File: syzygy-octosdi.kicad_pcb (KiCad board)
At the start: 2 copper layers, 50 x 100 mm, 177 parts, among them CN1 QTH-020-01-F-D-DP-A, J1 Conn_02x03_Odd_Even, U1 LMH0344SQE_NOPB, U10 LMH0344SQE_NOPB, U11 STM32G031G8Ux, U2 LMH0344SQE_NOPB, U3 GS2988-INE3, U4 GS2988-INE3, U5 PCAL6416AHF, U6 PCAL6416AHF, U7 GS2988-INE3, U8 GS2988-INE3, U9 LMH0344SQE_NOPB, X1 SX7DF148_500B20F30DNN

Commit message: implement schematic review feedback
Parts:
- U3, U4, U7, U8: value GS2988-INE3 -> ~
- X1: value SX7DF148_500B20F30DNN -> ~

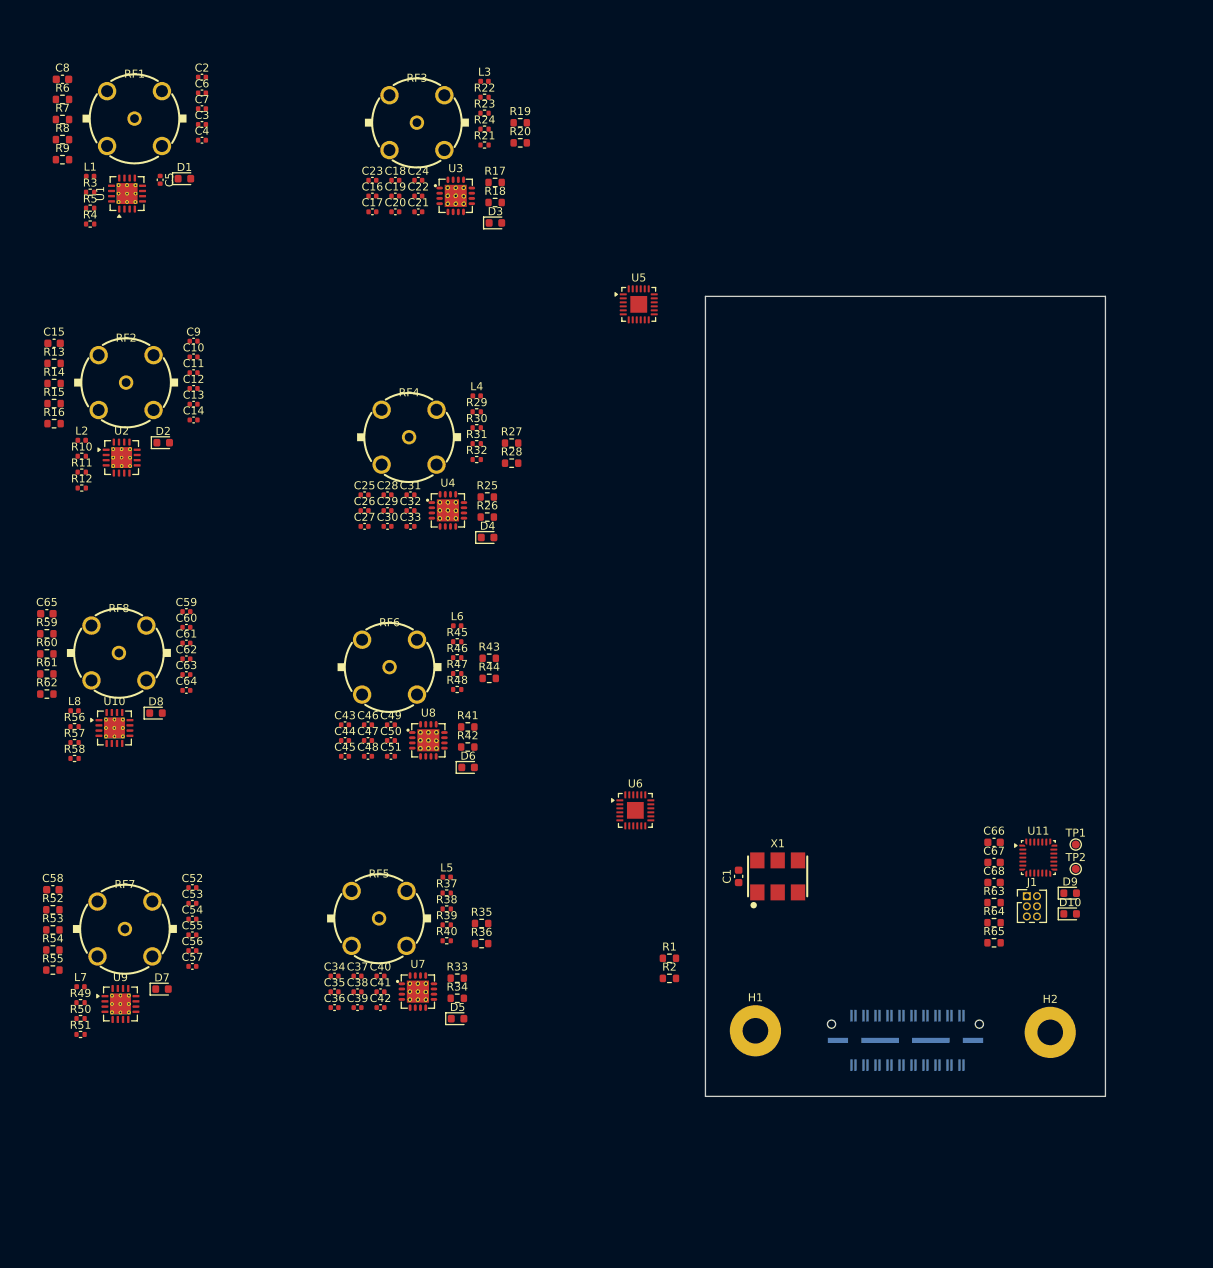
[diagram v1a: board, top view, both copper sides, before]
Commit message: substitute bnc connector for better max freq
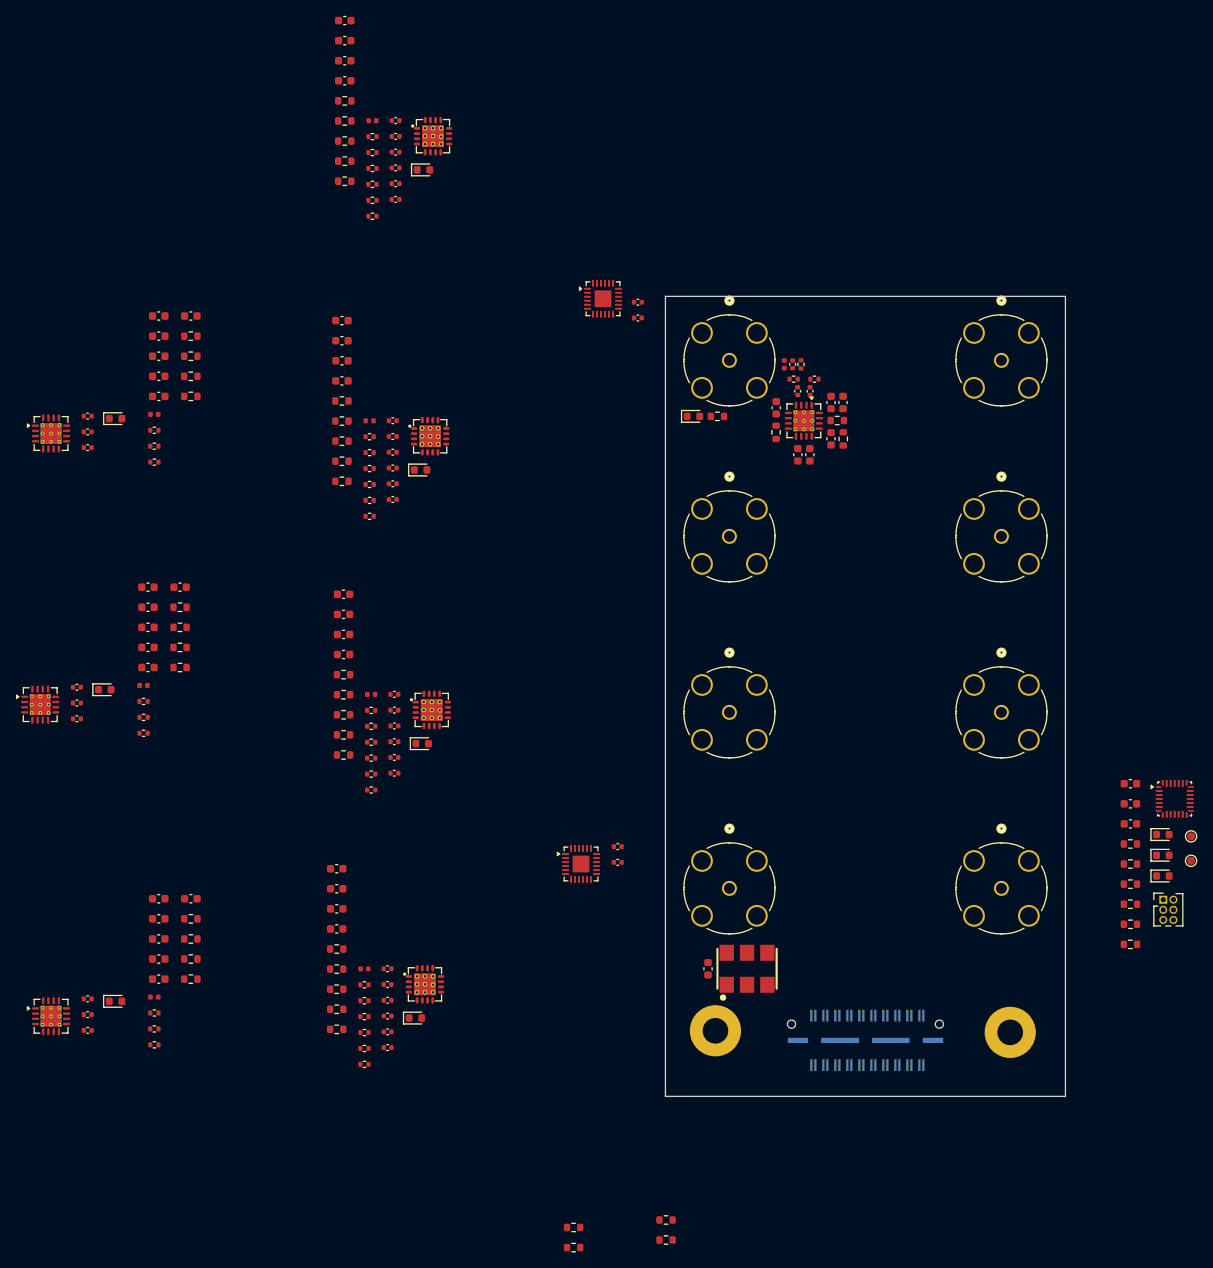
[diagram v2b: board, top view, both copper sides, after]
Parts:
- removed RF1, RF2, RF3, RF4, RF5, RF6, RF7, RF8: DOSIN-801-0057, JLCImport:DOSIN-801-0057
- added C10: 100n, Capacitor_SMD:C_0603_1608Metric, F.Cu at (120.7, 67.8)
- added C18: 100n, Capacitor_SMD:C_0603_1608Metric, F.Cu at (36.7, 62.5)
- added C19: 100n, Capacitor_SMD:C_0603_1608Metric, F.Cu at (40.7, 52.5)
- added C24: 100n, Capacitor_SMD:C_0402_1005Metric, F.Cu at (66.3, 37.9)
- added C34: 100n, Capacitor_SMD:C_0402_1005Metric, F.Cu at (65.9, 75.4)
- added C40: 100n, Capacitor_SMD:C_0402_1005Metric, F.Cu at (96.6, 50.7)
- added C41: 100n, Capacitor_SMD:C_0402_1005Metric, F.Cu at (96.6, 52.7)
- added C42: 100n, Capacitor_SMD:C_0402_1005Metric, F.Cu at (94.0, 118.8)
- added C43: 100n, Capacitor_SMD:C_0402_1005Metric, F.Cu at (94.0, 120.8)
- added C48: 100n, Capacitor_SMD:C_0402_1005Metric, F.Cu at (65.3, 143.9)
- added C58: 100n, Capacitor_SMD:C_0402_1005Metric, F.Cu at (66.1, 109.6)
- added C71: 100n, Capacitor_SMD:C_0603_1608Metric, F.Cu at (36.7, 135.3)
- added C72: 100n, Capacitor_SMD:C_0603_1608Metric, F.Cu at (40.7, 125.3)
- added C80: 100n, Capacitor_SMD:C_0603_1608Metric, F.Cu at (35.3, 96.4)
- added C81: 100n, Capacitor_SMD:C_0603_1608Metric, F.Cu at (39.3, 86.3)
- added C9: 100n, Capacitor_SMD:C_0603_1608Metric, F.Cu at (120.7, 63.3)
- added D11: LED, LED_SMD:LED_0603_1608Metric, F.Cu at (162.2, 122.5)
- added J1: Conn_Coaxial, JLCImport:CONN_73171-1900_MOL, F.Cu at (108.0, 58.0)
- added J10: Conn_Coaxial, JLCImport:CONN_73171-1900_MOL, F.Cu at (142.0, 124.0)
- added J2: Conn_Coaxial, JLCImport:CONN_73171-1900_MOL, F.Cu at (142.0, 58.0)
- added J3: Conn_Coaxial, JLCImport:CONN_73171-1900_MOL, F.Cu at (108.0, 80.0)
- added J5: Conn_Coaxial, JLCImport:CONN_73171-1900_MOL, F.Cu at (142.0, 80.0)
- added J6: Conn_Coaxial, JLCImport:CONN_73171-1900_MOL, F.Cu at (108.0, 102.0)
- added J7: Conn_Coaxial, JLCImport:CONN_73171-1900_MOL, F.Cu at (142.0, 102.0)
- added J8: Conn_Coaxial, JLCImport:CONN_73171-1900_MOL, F.Cu at (108.0, 124.0)
- added R19: 49.9, Resistor_SMD:R_0402_1005Metric, F.Cu at (63.4, 38.0)
- added R2: 10k, Resistor_SMD:R_0603_1608Metric, F.Cu at (88.5, 168.9)
- added R20: 49.9, Resistor_SMD:R_0402_1005Metric, F.Cu at (63.4, 40.0)
- added R27: 10k, Resistor_SMD:R_0603_1608Metric, F.Cu at (59.9, 35.6)
- added R30: 49.9, Resistor_SMD:R_0402_1005Metric, F.Cu at (63.0, 75.5)
- added R31: 49.9, Resistor_SMD:R_0402_1005Metric, F.Cu at (63.0, 77.5)
- added R38: 10k, Resistor_SMD:R_0603_1608Metric, F.Cu at (59.6, 73.1)
- added R4: 10k, Resistor_SMD:R_0603_1608Metric, F.Cu at (88.5, 166.4)
- added R41: 49.9, Resistor_SMD:R_0402_1005Metric, F.Cu at (62.4, 144.0)
- added R42: 49.9, Resistor_SMD:R_0402_1005Metric, F.Cu at (62.4, 146.0)
- added R49: 10k, Resistor_SMD:R_0603_1608Metric, F.Cu at (58.9, 141.6)
- added R52: 49.9, Resistor_SMD:R_0402_1005Metric, F.Cu at (63.2, 109.7)
- added R53: 49.9, Resistor_SMD:R_0402_1005Metric, F.Cu at (63.2, 111.7)
- added R60: 10k, Resistor_SMD:R_0603_1608Metric, F.Cu at (59.8, 107.3)
- added R80: 10k, Resistor_SMD:R_0603_1608Metric, F.Cu at (158.1, 128.5)
- added R81: 10k, Resistor_SMD:R_0603_1608Metric, F.Cu at (158.1, 126.0)
- added R82: 4k7, Resistor_SMD:R_0603_1608Metric, F.Cu at (158.1, 131.0)
- C1: value 10n -> 100n
- C14: renamed from C12; value 100n -> 1u; footprint Capacitor_SMD:C_0402_1005Metric -> Capacitor_SMD:C_0603_1608Metric
- C15: renamed from C13; footprint Capacitor_SMD:C_0402_1005Metric -> Capacitor_SMD:C_0603_1608Metric
- C16: renamed from C14; footprint Capacitor_SMD:C_0402_1005Metric -> Capacitor_SMD:C_0603_1608Metric
- C22: renamed from C18; footprint Capacitor_SMD:C_0402_1005Metric -> Capacitor_SMD:C_0603_1608Metric
- C23: renamed from C19; footprint Capacitor_SMD:C_0402_1005Metric -> Capacitor_SMD:C_0603_1608Metric
- C25: renamed from C20; footprint Capacitor_SMD:C_0402_1005Metric -> Capacitor_SMD:C_0603_1608Metric
- C29: renamed from C24; footprint Capacitor_SMD:C_0402_1005Metric -> Capacitor_SMD:C_0603_1608Metric
- C32: renamed from C27; footprint Capacitor_SMD:C_0402_1005Metric -> Capacitor_SMD:C_0603_1608Metric
- C33: renamed from C28; footprint Capacitor_SMD:C_0402_1005Metric -> Capacitor_SMD:C_0603_1608Metric
- C35: renamed from C29; footprint Capacitor_SMD:C_0402_1005Metric -> Capacitor_SMD:C_0603_1608Metric
- C39: renamed from C33; footprint Capacitor_SMD:C_0402_1005Metric -> Capacitor_SMD:C_0603_1608Metric
- C46: renamed from C36; footprint Capacitor_SMD:C_0402_1005Metric -> Capacitor_SMD:C_0603_1608Metric
- C47: renamed from C37; footprint Capacitor_SMD:C_0402_1005Metric -> Capacitor_SMD:C_0603_1608Metric
- C49: renamed from C38; footprint Capacitor_SMD:C_0402_1005Metric -> Capacitor_SMD:C_0603_1608Metric
- C5: value 100n -> 1u; footprint Capacitor_SMD:C_0402_1005Metric -> Capacitor_SMD:C_0603_1608Metric
- C53: renamed from C42; footprint Capacitor_SMD:C_0402_1005Metric -> Capacitor_SMD:C_0603_1608Metric
- C56: renamed from C45; footprint Capacitor_SMD:C_0402_1005Metric -> Capacitor_SMD:C_0603_1608Metric
- C57: renamed from C46; footprint Capacitor_SMD:C_0402_1005Metric -> Capacitor_SMD:C_0603_1608Metric
- C59: renamed from C47; footprint Capacitor_SMD:C_0402_1005Metric -> Capacitor_SMD:C_0603_1608Metric
- C6, C7: footprint Capacitor_SMD:C_0402_1005Metric -> Capacitor_SMD:C_0603_1608Metric
- C63: renamed from C51; footprint Capacitor_SMD:C_0402_1005Metric -> Capacitor_SMD:C_0603_1608Metric
- C67: renamed from C55; value 100n -> 1u; footprint Capacitor_SMD:C_0402_1005Metric -> Capacitor_SMD:C_0603_1608Metric
- C68: renamed from C56; footprint Capacitor_SMD:C_0402_1005Metric -> Capacitor_SMD:C_0603_1608Metric
- C69: renamed from C57; footprint Capacitor_SMD:C_0402_1005Metric -> Capacitor_SMD:C_0603_1608Metric
- C76: renamed from C62; value 100n -> 1u; footprint Capacitor_SMD:C_0402_1005Metric -> Capacitor_SMD:C_0603_1608Metric
- C77: renamed from C63; footprint Capacitor_SMD:C_0402_1005Metric -> Capacitor_SMD:C_0603_1608Metric
- C78: renamed from C64; footprint Capacitor_SMD:C_0402_1005Metric -> Capacitor_SMD:C_0603_1608Metric
- U3, U4, U7, U8: value ~ -> GS2988-INE3
- X1: value ~ -> SX7DF148_500B20F30DNN
- moved C8 105.6 mm to (122.2, 63.3), turned to 90 degrees
- moved R10 104.5 mm to (122.2, 67.8), turned to -90 degrees
- moved R11 102.2 mm to (121.5, 65.5)
- moved R9 97.4 mm to (113.8, 67.0), turned to -90 degrees
- moved R6 92.6 mm to (118.6, 60.4)
- moved R5 91.4 mm to (117.0, 58.5), turned to -90 degrees
- moved R8 91.0 mm to (106.5, 65.0), turned to 180 degrees
- moved R7 90.5 mm to (116.0, 60.4)
- moved L1 89.9 mm to (114.8, 58.5), turned to -90 degrees
- moved U1 89.2 mm to (117.3, 65.5), turned to -90 degrees
- moved C6 88.4 mm to (118.0, 69.8), turned to -90 degrees
- moved C7 86.1 mm to (116.5, 69.8), turned to -90 degrees
- moved C3 83.0 mm to (118.1, 61.9), turned to -90 degrees
- moved C5 82.1 mm to (113.8, 63.9)
- moved C2 82.1 mm to (115.9, 58.5), turned to -90 degrees
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- renumbered C9 to C11, C10 to C12, C11 to C13, C15 to C17, C16 to C20, C17 to C21, C21 to C26, C22 to C27, C23 to C28, C25 to C30, C26 to C31, C30 to C36, C31 to C37, C32 to C38, C34 to C44, C35 to C45, C39 to C50, C40 to C51, C41 to C52, C43 to C54, C44 to C55, C48 to C60, C49 to C61, C50 to C62, C52 to C64, C53 to C65, C54 to C66, C58 to C70, C59 to C73, C60 to C74, C61 to C75, C65 to C79, C66 to C82, C67 to C83, C68 to C84, J1 to J9, R8 to R10, R9 to R11, R10 to R12, R11 to R13, R12 to R14, R13 to R15, R14 to R16, R15 to R17, R16 to R18, R18 to R21, R17 to R22, R19 to R23, R20 to R24, R21 to R25, R22 to R26, R23 to R28, R24 to R29, R2 to R3, R26 to R32, R25 to R33, R27 to R34, R28 to R35, R29 to R36, R30 to R37, R31 to R39, R32 to R40, R34 to R43, R33 to R44, R35 to R45, R36 to R46, R37 to R47, R38 to R48, R3 to R5, R39 to R50, R40 to R51, R42 to R54, R41 to R55, R43 to R56, R44 to R57, R45 to R58, R46 to R59, R4 to R6, R47 to R61, R48 to R62, R49 to R63, R50 to R64, R51 to R65, R52 to R66, R53 to R67, R54 to R68, R55 to R69, R5 to R7, R56 to R70, R57 to R71, R58 to R72, R59 to R73, R60 to R74, R61 to R75, R62 to R76, R63 to R77, R64 to R78, R65 to R79, R6 to R8, R7 to R9
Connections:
- R10 pad 2: GND -> /~{VIO_GOOD}
- R17 pad 2: GND -> /~{VIO_GOOD}
- R68 pad 2: GND -> /~{VIO_GOOD}
- R75 pad 2: GND -> /~{VIO_GOOD}
- U11 pad 7: unconnected-(U11-PA1-Pad7) -> /VIO
- U11 pad 8: unconnected-(U11-PA2-Pad8) -> /VIO_GOOD
- U11 pad 9: unconnected-(U11-PA3-Pad9) -> /~{VIO_GOOD}
- U6 pad 18: /VIO -> +3V3
- X1 pad 1: unconnected-(X1-tri-state-Pad1) -> /VIO_GOOD

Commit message: split gpio expanders by inputs/outputs instead of quads
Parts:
- removed the C38 at (65.9, 73.4)
- removed the C39 at (59.6, 60.6)
- removed the C42 at (94.0, 118.8)
- removed the C43 at (94.0, 120.8)
- removed J10: Conn_Coaxial, JLCImport:CONN_73171-1900_MOL
- removed the R33 at (59.6, 63.1)
- removed the R34 at (59.6, 68.1)
- removed the R35 at (59.6, 70.6)
- removed the R36 at (63.0, 67.5)
- removed the R37 at (63.0, 69.5)
- removed the R38 at (59.6, 73.1)
- removed the R39 at (63.0, 71.5)
- removed the R40 at (63.0, 73.5)
- added C40: 100n, Capacitor_SMD:C_0402_1005Metric, F.Cu at (94.2, 102.9)
- added C41: 100n, Capacitor_SMD:C_0402_1005Metric, F.Cu at (94.2, 104.9)
- added C52: 10n, Capacitor_SMD:C_0402_1005Metric, F.Cu at (200.9, 78.9)
- added C53: 10n, Capacitor_SMD:C_0402_1005Metric, F.Cu at (200.9, 80.9)
- added J4: Conn_Coaxial, JLCImport:CONN_73171-1900_MOL, F.Cu at (243.1, 42.8)
- added R44: 49.9, Resistor_SMD:R_0402_1005Metric, F.Cu at (198.0, 80.9)
- added R45: 49.9, Resistor_SMD:R_0402_1005Metric, F.Cu at (198.0, 82.9)
- added R46: 1k, Resistor_SMD:R_0603_1608Metric, F.Cu at (194.5, 76.5)
- added R47: 750, Resistor_SMD:R_0603_1608Metric, F.Cu at (194.5, 79.0)
- added R48: 10k, Resistor_SMD:R_0603_1608Metric, F.Cu at (194.5, 81.5)
- added R49: 10k, Resistor_SMD:R_0603_1608Metric, F.Cu at (194.5, 84.0)
- added R50: 75, Resistor_SMD:R_0402_1005Metric, F.Cu at (198.0, 84.9)
- added R51: 75, Resistor_SMD:R_0402_1005Metric, F.Cu at (198.0, 86.9)
- C20, C60: value 10n -> C
- C21, C30, C31: value 10n -> 1u
- C22: value 4u7 -> 1u; footprint Capacitor_SMD:C_0603_1608Metric -> Capacitor_SMD:C_0402_1005Metric
- C23, C32, C35: value 4u7 -> 1u
- C24, C34: value 100n -> 4u7; footprint Capacitor_SMD:C_0402_1005Metric -> Capacitor_SMD:C_0603_1608Metric
- C26: value 10n -> 1u; footprint Capacitor_SMD:C_0402_1005Metric -> Capacitor_SMD:C_0603_1608Metric
- C27, C36, C37: value 10n -> 100n; footprint Capacitor_SMD:C_0402_1005Metric -> Capacitor_SMD:C_0603_1608Metric
- C28: value C -> 100n; footprint Capacitor_SMD:C_0402_1005Metric -> Capacitor_SMD:C_0603_1608Metric
- C29: value 4u7 -> C; footprint Capacitor_SMD:C_0603_1608Metric -> Capacitor_SMD:C_0402_1005Metric
- C54, C55, C61: value 10n -> 4u7; footprint Capacitor_SMD:C_0402_1005Metric -> Capacitor_SMD:C_0603_1608Metric
- C56: value 4u7 -> 100n; footprint Capacitor_SMD:C_0603_1608Metric -> Capacitor_SMD:C_0402_1005Metric
- C58: value 100n -> 10n
- C59, C63, C68, C69, C78: value 4u7 -> 10n; footprint Capacitor_SMD:C_0603_1608Metric -> Capacitor_SMD:C_0402_1005Metric
- C62, C73: value C -> 10n
- C64: value C -> 4u7; footprint Capacitor_SMD:C_0402_1005Metric -> Capacitor_SMD:C_0603_1608Metric
- C65, C74, C75: value 1u -> 4u7; footprint Capacitor_SMD:C_0402_1005Metric -> Capacitor_SMD:C_0603_1608Metric
- C66: value 1u -> 100n
- C67: value 1u -> 4u7
- C70: value 1u -> C; footprint Capacitor_SMD:C_0603_1608Metric -> Capacitor_SMD:C_0402_1005Metric
- C71, C81: value 100n -> 4u7
- C72: value 100n -> 10n; footprint Capacitor_SMD:C_0603_1608Metric -> Capacitor_SMD:C_0402_1005Metric
- C76: value 1u -> 100n; footprint Capacitor_SMD:C_0603_1608Metric -> Capacitor_SMD:C_0402_1005Metric
- C79: value 1u -> 10n; footprint Capacitor_SMD:C_0603_1608Metric -> Capacitor_SMD:C_0402_1005Metric
- C80: value 100n -> C; footprint Capacitor_SMD:C_0603_1608Metric -> Capacitor_SMD:C_0402_1005Metric
- L3, L4: value 5n6 -> 3n9
- L7, L8: value 3n9 -> 5n6
- R19, R20, R53: value 49.9 -> 75
- R21: value 1k -> 37.4; footprint Resistor_SMD:R_0603_1608Metric -> Resistor_SMD:R_0402_1005Metric
- R22: value 750 -> 1k
- R25: value 75 -> 0; footprint Resistor_SMD:R_0402_1005Metric -> Resistor_SMD:R_0603_1608Metric
- R27, R75: value 10k -> 75; footprint Resistor_SMD:R_0603_1608Metric -> Resistor_SMD:R_0402_1005Metric
- R28: value 75 -> 37.4
- R29: value 75 -> 1k; footprint Resistor_SMD:R_0402_1005Metric -> Resistor_SMD:R_0603_1608Metric
- R30, R31, R52: value 49.9 -> 10k; footprint Resistor_SMD:R_0402_1005Metric -> Resistor_SMD:R_0603_1608Metric
- R32: value 1k -> 0
- R54, R73: value 1k -> 75; footprint Resistor_SMD:R_0603_1608Metric -> Resistor_SMD:R_0402_1005Metric
- R55: value 750 -> 49.9; footprint Resistor_SMD:R_0603_1608Metric -> Resistor_SMD:R_0402_1005Metric
- R56, R67: value 10k -> 49.9; footprint Resistor_SMD:R_0603_1608Metric -> Resistor_SMD:R_0402_1005Metric
- R57, R68: value 10k -> 1k
- R58: value 75 -> 750; footprint Resistor_SMD:R_0402_1005Metric -> Resistor_SMD:R_0603_1608Metric
- R59, R63, R70, R71: value 75 -> 10k; footprint Resistor_SMD:R_0402_1005Metric -> Resistor_SMD:R_0603_1608Metric
- R65, R72: value 37.4 -> 75
- R66: value 1k -> 49.9; footprint Resistor_SMD:R_0603_1608Metric -> Resistor_SMD:R_0402_1005Metric
- R69: value 0 -> 750
- R76: value 0 -> 75; footprint Resistor_SMD:R_0603_1608Metric -> Resistor_SMD:R_0402_1005Metric
- U10, U9: value LMH0344SQE_NOPB -> GS2988-INE3; footprint Package_DFN_QFN:Texas_RUM0016A_WQFN-16-1EP_4x4mm_P0.65mm_EP2.6x2.6mm_ThermalVias -> JLCImport:GS2988-INE3
- U3, U4: value GS2988-INE3 -> LMH0344SQE_NOPB; footprint JLCImport:GS2988-INE3 -> Package_DFN_QFN:Texas_RUM0016A_WQFN-16-1EP_4x4mm_P0.65mm_EP2.6x2.6mm_ThermalVias
- moved U9 221.5 mm to (226.5, 52.2)
- moved C11 219.3 mm to (246.6, 78.9)
- moved C12 219.3 mm to (246.6, 80.9)
- moved C13 219.3 mm to (246.6, 82.9)
- moved C14 219.3 mm to (255.5, 66.4)
- moved C15 219.3 mm to (255.5, 68.9)
- moved C16 219.3 mm to (255.5, 71.4)
- moved C17 219.3 mm to (255.5, 73.9)
- moved C18 219.3 mm to (255.5, 76.5)
- moved L2 219.3 mm to (255.0, 78.7)
- moved R12 219.3 mm to (255.0, 80.7)
- moved R13 219.3 mm to (255.0, 82.7)
- moved R14 219.3 mm to (255.0, 84.7)
- moved U2 219.3 mm to (242.0, 81.1)
- moved C19 219.3 mm to (259.5, 66.4)
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- renumbered C40 to C38, C41 to C39, C44 to C42, C45 to C43, C46 to C44, C47 to C45, C48 to C46, C49 to C47, C50 to C48, C51 to C49, C52 to C50, C53 to C51, R41 to R33, R42 to R34, R43 to R35, R44 to R36, R45 to R37, R46 to R38, R47 to R39, R48 to R40, R49 to R41, R50 to R42, R51 to R43
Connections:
- net /Quad/SDI In 1/BYPASS renamed /Inputs/SDI In 1/BYPASS
- net /Quad/SDI In 1/MUTE renamed /Inputs/SDI In 1/MUTE
- net /Quad/SDI In 1/~{CD} renamed /Inputs/SDI In 1/~{CD}
- C20 pad 1: +3V3 -> Net-(J3-In)
- C20 pad 2: GND -> Net-(C20-Pad2)
- C21 pad 1: +3V3 -> Net-(C20-Pad2)
- C21 pad 2: GND -> Net-(U3-SDI)
- C22 pad 1: /TX0.P -> Net-(C22-Pad1)
- C22 pad 2: Net-(U3-DDI) -> Net-(U3-SDI#)
- C23 pad 1: /TX0.N -> Net-(U3-AEC+)
- C23 pad 2: Net-(U3-~{DDI}) -> Net-(U3-AEC-)
- C24 pad 1: Net-(C24-Pad1) -> Net-(U3-SDO)
- C24 pad 2: GND -> /RX2.P
- C25 pad 1: Net-(U3-~{SDO}) -> Net-(U3-SDO#)
- C25 pad 2: Net-(C25-Pad2) -> /RX2.N
- C28 pad 1: Net-(U3-SDO) -> +3V3
- C28 pad 2: Net-(C28-Pad2) -> GND
- C29 pad 1: Net-(C28-Pad2) -> Net-(J4-In)
- C29 pad 2: Net-(J3-In) -> Net-(C29-Pad2)
- C30 pad 1: +3V3 -> Net-(C29-Pad2)
- C30 pad 2: GND -> Net-(U4-SDI)
- C31 pad 1: +3V3 -> Net-(C31-Pad1)
- C31 pad 2: GND -> Net-(U4-SDI#)
- C32 pad 1: /TX1.P -> Net-(U4-AEC+)
- C32 pad 2: Net-(U4-DDI) -> Net-(U4-AEC-)
- C33 pad 1: /TX1.N -> Net-(U4-SDO)
- C33 pad 2: Net-(U4-~{DDI}) -> /RX3.P
- C34 pad 1: Net-(C34-Pad1) -> Net-(U4-SDO#)
- C34 pad 2: GND -> /RX3.N
- C35 pad 1: Net-(U4-~{SDO}) -> +3V3
- C35 pad 2: Net-(C35-Pad2) -> GND
- C44 pad 1: /TX3.P -> /TX0.P
- C45 pad 1: /TX3.N -> /TX0.N
- C54 pad 1: +3V3 -> /TX1.P
- C54 pad 2: GND -> Net-(U8-DDI)
- C55 pad 1: +3V3 -> /TX1.N
- C55 pad 2: GND -> Net-(U8-~{DDI})
- C56 pad 1: /TX2.P -> Net-(C56-Pad1)
- C56 pad 2: Net-(U8-DDI) -> GND
- C57 pad 1: /TX2.N -> Net-(U8-~{SDO})
- C57 pad 2: Net-(U8-~{DDI}) -> Net-(C57-Pad2)
- C58 pad 1: Net-(C58-Pad1) -> +3V3
- C59 pad 1: Net-(U8-~{SDO}) -> +3V3
- C59 pad 2: Net-(C59-Pad2) -> GND
- C60 pad 1: +3V3 -> Net-(U8-SDO)
- C60 pad 2: GND -> Net-(C60-Pad2)
- C61 pad 1: +3V3 -> Net-(C60-Pad2)
- C61 pad 2: GND -> Net-(J6-In)
- C62 pad 1: Net-(U8-SDO) -> +3V3
- C62 pad 2: Net-(C62-Pad2) -> GND
- C63 pad 1: Net-(C62-Pad2) -> +3V3
- C63 pad 2: Net-(J6-In) -> GND
- C64 pad 1: Net-(J7-In) -> /TX2.P
- C64 pad 2: Net-(C64-Pad2) -> Net-(U9-DDI)
- C65 pad 1: Net-(C64-Pad2) -> /TX2.N
- C65 pad 2: Net-(U9-SDI) -> Net-(U9-~{DDI})
- C66 pad 2: Net-(U9-SDI#) -> GND
- C67 pad 1: Net-(U9-AEC+) -> Net-(U9-~{SDO})
- C67 pad 2: Net-(U9-AEC-) -> Net-(C67-Pad2)
- C68 pad 1: Net-(U9-SDO) -> +3V3
- C68 pad 2: /RX3.P -> GND
- C69 pad 1: Net-(U9-SDO#) -> +3V3
- C69 pad 2: /RX3.N -> GND
- C70 pad 1: +3V3 -> Net-(U9-SDO)
- C70 pad 2: GND -> Net-(C70-Pad2)
- C71 pad 1: +3V3 -> Net-(C70-Pad2)
- C71 pad 2: GND -> Net-(J7-In)
- C73 pad 1: Net-(J8-In) -> +3V3
- C73 pad 2: Net-(C73-Pad2) -> GND
- C74 pad 1: Net-(C73-Pad2) -> /TX3.P
- C74 pad 2: Net-(U10-SDI) -> Net-(U10-DDI)
- C75 pad 1: Net-(C75-Pad1) -> /TX3.N
- C75 pad 2: Net-(U10-SDI#) -> Net-(U10-~{DDI})
- C76 pad 1: Net-(U10-AEC+) -> Net-(C76-Pad1)
- C76 pad 2: Net-(U10-AEC-) -> GND
- C77 pad 1: Net-(U10-SDO) -> Net-(U10-~{SDO})
- C77 pad 2: /RX2.P -> Net-(C77-Pad2)
- C78 pad 1: Net-(U10-SDO#) -> +3V3
- C78 pad 2: /RX2.N -> GND
- C80 pad 1: +3V3 -> Net-(U10-SDO)
- C80 pad 2: GND -> Net-(C80-Pad2)
- C81 pad 1: +3V3 -> Net-(C80-Pad2)
- C81 pad 2: GND -> Net-(J8-In)
- D2 pad 1: /Quad/SDI In 2/~{CD} -> /Inputs/SDI In 2/~{CD}
- D3 pad 1: /Quad/SDI Out 1/~{OSP} -> /Inputs/SDI In 3/~{CD}
- D4 pad 1: /Quad/SDI Out 2/~{OSP} -> /Inputs/SDI In 4/~{CD}
- D5 pad 1: /Quad1/SDI Out 2/~{OSP} -> /Outputs/SDI Out 1/~{OSP}
- D6 pad 1: /Quad1/SDI Out 1/~{OSP} -> /Outputs/SDI Out 2/~{OSP}
- D7 pad 1: /Quad1/SDI In 2/~{CD} -> /Outputs/SDI Out 3/~{OSP}
- D8 pad 1: /Quad1/SDI In 1/~{CD} -> /Outputs/SDI Out 4/~{OSP}
- J2 pad 1: Net-(J1-In) -> Net-(J2-In)
- J3 pad 1: Net-(J1-In) -> Net-(J3-In)
- J5 pad 1: Net-(J1-In) -> Net-(J5-In)
- J6 pad 1: Net-(J1-In) -> Net-(J6-In)
- J7 pad 1: Net-(J1-In) -> Net-(J7-In)
- J8 pad 1: Net-(J1-In) -> Net-(J8-In)
- L3 pad 1: Net-(U3-SDO) -> Net-(J3-In)
- L3 pad 2: Net-(C28-Pad2) -> Net-(C20-Pad2)
- L4 pad 1: Net-(U4-SDO) -> Net-(J4-In)
- L4 pad 2: Net-(C38-Pad2) -> Net-(C29-Pad2)
- L6 pad 2: Net-(C62-Pad2) -> Net-(C60-Pad2)
- L7 pad 1: Net-(J7-In) -> Net-(U9-SDO)
- L7 pad 2: Net-(C64-Pad2) -> Net-(C70-Pad2)
- L8 pad 1: Net-(J8-In) -> Net-(U10-SDO)
- L8 pad 2: Net-(C73-Pad2) -> Net-(C80-Pad2)
- R16 pad 1: /Quad/SDI In 2/BYPASS -> /Inputs/SDI In 2/BYPASS
- R17 pad 1: /Quad/SDI In 2/MUTE -> /Inputs/SDI In 2/MUTE
- R18 pad 1: /Quad/SDI In 2/~{CD} -> /Inputs/SDI In 2/~{CD}
- R18 pad 2: /Quad/SDI In 2/MUTE -> /Inputs/SDI In 2/MUTE
- R19 pad 1: Net-(U3-DDI) -> Net-(J3-In)
- R19 pad 2: Net-(C24-Pad1) -> Net-(C20-Pad2)
- R20 pad 1: Net-(C24-Pad1) -> Net-(C20-Pad2)
- R20 pad 2: Net-(U3-~{DDI}) -> GND
- R21 pad 1: +3V3 -> GND
- R21 pad 2: Net-(D3-A) -> Net-(C22-Pad1)
- R22 pad 2: Net-(U3-REST) -> Net-(D3-A)
- R23 pad 1: /Quad/SDI Out 1/SD/~{HD} -> /Inputs/SDI In 3/BYPASS
- R24 pad 1: /Quad/SDI Out 1/~{EQ_EN} -> /Inputs/SDI In 3/MUTE
- R24 pad 2: GND -> /~{VIO_GOOD}
- R25 pad 1: +3V3 -> /Inputs/SDI In 3/~{CD}
- R25 pad 2: Net-(U3-~{SDO}) -> /Inputs/SDI In 3/MUTE
- R26 pad 1: Net-(C25-Pad2) -> Net-(J4-In)
- R26 pad 2: GND -> Net-(C29-Pad2)
- R27 pad 1: /VIO_GOOD -> Net-(C29-Pad2)
- R27 pad 2: /Quad/SDI Out 1/~{DISABLE} -> GND
- R28 pad 1: +3V3 -> GND
- R28 pad 2: Net-(U3-SDO) -> Net-(C31-Pad1)
- R29 pad 1: Net-(U3-SDO) -> +3V3
- R29 pad 2: Net-(C28-Pad2) -> Net-(D4-A)
- R30 pad 1: Net-(U4-DDI) -> /Inputs/SDI In 4/BYPASS
- R30 pad 2: Net-(C34-Pad1) -> GND
- R31 pad 1: Net-(C34-Pad1) -> /Inputs/SDI In 4/MUTE
- R31 pad 2: Net-(U4-~{DDI}) -> /~{VIO_GOOD}
- R32 pad 1: +3V3 -> /Inputs/SDI In 4/~{CD}
- R32 pad 2: Net-(D4-A) -> /Inputs/SDI In 4/MUTE
- R37 pad 1: /Quad1/SDI Out 2/SD/~{HD} -> /Outputs/SDI Out 1/SD/~{HD}
- R38 pad 1: /Quad1/SDI Out 2/~{EQ_EN} -> /Outputs/SDI Out 1/~{EQ_EN}
- R41 pad 2: /Quad1/SDI Out 2/~{DISABLE} -> /Outputs/SDI Out 1/~{DISABLE}
- R52 pad 1: Net-(U8-DDI) -> /VIO_GOOD
- R52 pad 2: Net-(C58-Pad1) -> /Outputs/SDI Out 2/~{DISABLE}
- R53 pad 1: Net-(C58-Pad1) -> +3V3
- R53 pad 2: Net-(U8-~{DDI}) -> Net-(U8-SDO)
- R54 pad 1: +3V3 -> Net-(U8-SDO)
- R54 pad 2: Net-(D6-A) -> Net-(C60-Pad2)
- R55 pad 1: +3V3 -> Net-(U9-DDI)
- R55 pad 2: Net-(U8-REST) -> Net-(C66-Pad1)
- R56 pad 1: /Quad1/SDI Out 1/SD/~{HD} -> Net-(C66-Pad1)
- R56 pad 2: GND -> Net-(U9-~{DDI})
- R57 pad 1: /Quad1/SDI Out 1/~{EQ_EN} -> +3V3
- R57 pad 2: GND -> Net-(D7-A)
- R58 pad 2: Net-(U8-~{SDO}) -> Net-(U9-REST)
- R59 pad 1: Net-(C59-Pad2) -> /Outputs/SDI Out 3/SD/~{HD}
- R60 pad 1: /VIO_GOOD -> /Outputs/SDI Out 3/~{EQ_EN}
- R60 pad 2: /Quad1/SDI Out 1/~{DISABLE} -> GND
- R61 pad 2: Net-(U8-SDO) -> Net-(U9-~{SDO})
- R62 pad 1: Net-(U8-SDO) -> Net-(C67-Pad2)
- R62 pad 2: Net-(C62-Pad2) -> GND
- R63 pad 1: Net-(J7-In) -> /VIO_GOOD
- R63 pad 2: Net-(C64-Pad2) -> /Outputs/SDI Out 3/~{DISABLE}
- R64 pad 1: Net-(C64-Pad2) -> +3V3
- R64 pad 2: GND -> Net-(U9-SDO)
- R65 pad 1: GND -> Net-(U9-SDO)
- R65 pad 2: Net-(C66-Pad1) -> Net-(C70-Pad2)
- R66 pad 1: +3V3 -> Net-(U10-DDI)
- R66 pad 2: Net-(D7-A) -> Net-(C76-Pad1)
- R67 pad 1: /Quad1/SDI In 2/BYPASS -> Net-(C76-Pad1)
- R67 pad 2: GND -> Net-(U10-~{DDI})
- R68 pad 1: /Quad1/SDI In 2/MUTE -> +3V3
- R68 pad 2: /~{VIO_GOOD} -> Net-(D8-A)
- R69 pad 1: /Quad1/SDI In 2/~{CD} -> +3V3
- R69 pad 2: /Quad1/SDI In 2/MUTE -> Net-(U10-REST)
- R70 pad 1: Net-(J8-In) -> /Outputs/SDI Out 4/SD/~{HD}
- R70 pad 2: Net-(C73-Pad2) -> GND
- R71 pad 1: Net-(C73-Pad2) -> /Outputs/SDI Out 4/~{EQ_EN}
- R72 pad 1: GND -> +3V3
- R72 pad 2: Net-(C75-Pad1) -> Net-(U10-~{SDO})
- R73 pad 1: +3V3 -> Net-(C77-Pad2)
- R73 pad 2: Net-(D8-A) -> GND
- R74 pad 1: /Quad1/SDI In 1/BYPASS -> /VIO_GOOD
- R74 pad 2: GND -> /Outputs/SDI Out 4/~{DISABLE}
- R75 pad 1: /Quad1/SDI In 1/MUTE -> +3V3
- R75 pad 2: /~{VIO_GOOD} -> Net-(U10-SDO)
- R76 pad 1: /Quad1/SDI In 1/~{CD} -> Net-(U10-SDO)
- R76 pad 2: /Quad1/SDI In 1/MUTE -> Net-(C80-Pad2)
- U10 pad 1: GND -> Net-(U10-DDI)
- U10 pad 10: Net-(U10-SDO#) -> /Outputs/SDI Out 4/SD/~{HD}
- U10 pad 11: Net-(U10-SDO) -> Net-(U10-~{SDO})
- U10 pad 12: GND -> Net-(U10-SDO)
- U10 pad 13: +3V3 -> unconnected-(U10-N/C-Pad13)
- U10 pad 14: /Quad1/SDI In 1/MUTE -> /Outputs/SDI Out 4/~{OSP}
- U10 pad 15: /Quad1/SDI In 1/~{CD} -> unconnected-(U10-N/C-Pad15)
- U10 pad 16: +3V3 -> /Outputs/SDI Out 4/~{EQ_EN}
- U10 pad 2: Net-(U10-SDI) -> Net-(U10-~{DDI})
- U10 pad 3: Net-(U10-SDI#) -> GND
- U10 pad 4: GND -> Net-(U10-REST)
- U10 pad 5: Net-(U10-AEC+) -> unconnected-(U10-N/C-Pad5)
- U10 pad 6: Net-(U10-AEC-) -> /Outputs/SDI Out 4/~{DISABLE}
- U10 pad 7: /Quad1/SDI In 1/BYPASS -> unconnected-(U10-N/C-Pad7)
- U10 pad 9: GND -> +3V3
- U2 pad 14: /Quad/SDI In 2/MUTE -> /Inputs/SDI In 2/MUTE
- U2 pad 15: /Quad/SDI In 2/~{CD} -> /Inputs/SDI In 2/~{CD}
- U2 pad 7: /Quad/SDI In 2/BYPASS -> /Inputs/SDI In 2/BYPASS
- U3 pad 1: Net-(U3-DDI) -> GND
- U3 pad 10: /Quad/SDI Out 1/SD/~{HD} -> Net-(U3-SDO#)
- U3 pad 11: Net-(U3-~{SDO}) -> Net-(U3-SDO)
- U3 pad 12: Net-(U3-SDO) -> GND
- U3 pad 13: unconnected-(U3-N/C-Pad13) -> +3V3
- U3 pad 14: /Quad/SDI Out 1/~{OSP} -> /Inputs/SDI In 3/MUTE
- U3 pad 15: unconnected-(U3-N/C-Pad15) -> /Inputs/SDI In 3/~{CD}
- U3 pad 16: /Quad/SDI Out 1/~{EQ_EN} -> +3V3
- U3 pad 2: Net-(U3-~{DDI}) -> Net-(U3-SDI)
- U3 pad 3: GND -> Net-(U3-SDI#)
- U3 pad 4: Net-(U3-REST) -> GND
- U3 pad 5: unconnected-(U3-N/C-Pad5) -> Net-(U3-AEC+)
- U3 pad 6: /Quad/SDI Out 1/~{DISABLE} -> Net-(U3-AEC-)
- U3 pad 7: unconnected-(U3-N/C-Pad7) -> /Inputs/SDI In 3/BYPASS
- U3 pad 9: +3V3 -> GND
- U4 pad 1: Net-(U4-DDI) -> GND
- U4 pad 10: /Quad/SDI Out 2/SD/~{HD} -> Net-(U4-SDO#)
- U4 pad 11: Net-(U4-~{SDO}) -> Net-(U4-SDO)
- U4 pad 12: Net-(U4-SDO) -> GND
- U4 pad 13: unconnected-(U4-N/C-Pad13) -> +3V3
- U4 pad 14: /Quad/SDI Out 2/~{OSP} -> /Inputs/SDI In 4/MUTE
- U4 pad 15: unconnected-(U4-N/C-Pad15) -> /Inputs/SDI In 4/~{CD}
- U4 pad 16: /Quad/SDI Out 2/~{EQ_EN} -> +3V3
- U4 pad 2: Net-(U4-~{DDI}) -> Net-(U4-SDI)
- U4 pad 3: GND -> Net-(U4-SDI#)
- U4 pad 4: Net-(U4-REST) -> GND
- U4 pad 5: unconnected-(U4-N/C-Pad5) -> Net-(U4-AEC+)
- U4 pad 6: /Quad/SDI Out 2/~{DISABLE} -> Net-(U4-AEC-)
- U4 pad 7: unconnected-(U4-N/C-Pad7) -> /Inputs/SDI In 4/BYPASS
- U4 pad 9: +3V3 -> GND
- U5 pad 10: /Quad/SDI In 2/BYPASS -> /Inputs/SDI In 3/BYPASS
- U5 pad 11: /Quad/SDI In 2/MUTE -> /Inputs/SDI In 3/MUTE
- U5 pad 12: /Quad/SDI In 2/~{CD} -> /Inputs/SDI In 3/~{CD}
- U5 pad 13: /Quad/SDI Out 2/SD/~{HD} -> unconnected-(U5-P1_3-Pad13)
- U5 pad 14: /Quad/SDI Out 2/~{DISABLE} -> /Inputs/SDI In 4/BYPASS
- U5 pad 15: /Quad/SDI Out 2/~{EQ_EN} -> /Inputs/SDI In 4/MUTE
- U5 pad 16: /Quad/SDI Out 2/~{OSP} -> /Inputs/SDI In 4/~{CD}
- U5 pad 4: /Quad/SDI Out 1/SD/~{HD} -> unconnected-(U5-P0_3-Pad4)
- U5 pad 5: /Quad/SDI Out 1/~{DISABLE} -> /Inputs/SDI In 2/BYPASS
- U5 pad 6: /Quad/SDI Out 1/~{EQ_EN} -> /Inputs/SDI In 2/MUTE
- U5 pad 7: /Quad/SDI Out 1/~{OSP} -> /Inputs/SDI In 2/~{CD}
- U6 pad 1: /Quad1/SDI In 1/BYPASS -> /Outputs/SDI Out 1/SD/~{HD}
- U6 pad 10: /Quad1/SDI In 2/BYPASS -> /Outputs/SDI Out 3/SD/~{HD}
- U6 pad 11: /Quad1/SDI In 2/MUTE -> /Outputs/SDI Out 3/~{DISABLE}
- U6 pad 12: /Quad1/SDI In 2/~{CD} -> /Outputs/SDI Out 3/~{EQ_EN}
- U6 pad 13: /Quad1/SDI Out 2/SD/~{HD} -> /Outputs/SDI Out 3/~{OSP}
- U6 pad 14: /Quad1/SDI Out 2/~{DISABLE} -> /Outputs/SDI Out 4/SD/~{HD}
- U6 pad 15: /Quad1/SDI Out 2/~{EQ_EN} -> /Outputs/SDI Out 4/~{DISABLE}
- U6 pad 16: /Quad1/SDI Out 2/~{OSP} -> /Outputs/SDI Out 4/~{EQ_EN}
- U6 pad 17: unconnected-(U6-P1_7-Pad17) -> /Outputs/SDI Out 4/~{OSP}
- U6 pad 2: /Quad1/SDI In 1/MUTE -> /Outputs/SDI Out 1/~{DISABLE}
- U6 pad 3: /Quad1/SDI In 1/~{CD} -> /Outputs/SDI Out 1/~{EQ_EN}
- U6 pad 4: /Quad1/SDI Out 1/SD/~{HD} -> /Outputs/SDI Out 1/~{OSP}
- U6 pad 5: /Quad1/SDI Out 1/~{DISABLE} -> /Outputs/SDI Out 2/SD/~{HD}
- U6 pad 6: /Quad1/SDI Out 1/~{EQ_EN} -> /Outputs/SDI Out 2/~{DISABLE}
- U6 pad 7: /Quad1/SDI Out 1/~{OSP} -> /Outputs/SDI Out 2/~{EQ_EN}
- U6 pad 8: unconnected-(U6-P0_7-Pad8) -> /Outputs/SDI Out 2/~{OSP}
- U7 pad 10: /Quad1/SDI Out 2/SD/~{HD} -> /Outputs/SDI Out 1/SD/~{HD}
- U7 pad 14: /Quad1/SDI Out 2/~{OSP} -> /Outputs/SDI Out 1/~{OSP}
- U7 pad 16: /Quad1/SDI Out 2/~{EQ_EN} -> /Outputs/SDI Out 1/~{EQ_EN}
- U7 pad 6: /Quad1/SDI Out 2/~{DISABLE} -> /Outputs/SDI Out 1/~{DISABLE}
- U8 pad 10: /Quad1/SDI Out 1/SD/~{HD} -> /Outputs/SDI Out 2/SD/~{HD}
- U8 pad 14: /Quad1/SDI Out 1/~{OSP} -> /Outputs/SDI Out 2/~{OSP}
- U8 pad 16: /Quad1/SDI Out 1/~{EQ_EN} -> /Outputs/SDI Out 2/~{EQ_EN}
- U8 pad 6: /Quad1/SDI Out 1/~{DISABLE} -> /Outputs/SDI Out 2/~{DISABLE}
- U9 pad 1: GND -> Net-(U9-DDI)
- U9 pad 10: Net-(U9-SDO#) -> /Outputs/SDI Out 3/SD/~{HD}
- U9 pad 11: Net-(U9-SDO) -> Net-(U9-~{SDO})
- U9 pad 12: GND -> Net-(U9-SDO)
- U9 pad 13: +3V3 -> unconnected-(U9-N/C-Pad13)
- U9 pad 14: /Quad1/SDI In 2/MUTE -> /Outputs/SDI Out 3/~{OSP}
- U9 pad 15: /Quad1/SDI In 2/~{CD} -> unconnected-(U9-N/C-Pad15)
- U9 pad 16: +3V3 -> /Outputs/SDI Out 3/~{EQ_EN}
- U9 pad 2: Net-(U9-SDI) -> Net-(U9-~{DDI})
- U9 pad 3: Net-(U9-SDI#) -> GND
- U9 pad 4: GND -> Net-(U9-REST)
- U9 pad 5: Net-(U9-AEC+) -> unconnected-(U9-N/C-Pad5)
- U9 pad 6: Net-(U9-AEC-) -> /Outputs/SDI Out 3/~{DISABLE}
- U9 pad 7: /Quad1/SDI In 2/BYPASS -> unconnected-(U9-N/C-Pad7)
- U9 pad 9: GND -> +3V3
